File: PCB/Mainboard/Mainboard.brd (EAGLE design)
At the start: 39.1 x 39.1 mm, 18 parts

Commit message: Redesign
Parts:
- removed C3, C4, C5: 20nF, rcl:C0603
- removed DOWN, LEFT, RIGHT, UP: TASTER, button:TASTER
- removed MCU: ATTINY1614/16/17, ATTINY161x:QFN24-4X4
- removed U$1, U$2, U$3, U$4: MOLEX-STACKINGHEADER, Molex-53307-1071:53307-1071
- added JP1: (no value), pinhead:1X02/90
- added LED1, LED2: (no value), led:CHIP-LED0805
- added LEG_0: ATTINY1614, HeRo:SOIC14
- added R5, R6: (no value), rcl:R0805
- added SERVO_0: SERVO_X3, HeRo:2X03/90
- C1: value 100nF -> (none); device rcl:C0603 -> rcl:C0805
- C2: value 20nF -> (none); device rcl:C0603 -> rcl:C0805
- R1, R2, R3, R4: value 1k -> (none); device rcl:R0603 -> rcl:R0805
- moved R2 32.6 mm to (3.81, 4.45), turned to 0 degrees
- moved C1 25.7 mm to (8.26, 4.45), flipped to the top, turned to 180 degrees
- moved C2 17.3 mm to (17.1, 17.8)
- moved R4 13.0 mm to (15.6, 10.8), turned to 45 degrees
- moved R3 8.67 mm to (14.9, 13.3), turned to 45 degrees
- moved R1 6.99 mm to (12.7, 4.45), turned to 180 degrees
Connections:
- removed net ADD0: MCU.7, U$1.P$6
- removed net ADD1: MCU.8, U$1.P$7
- removed net ADD2: MCU.9, U$1.P$8
- removed net ADD3: MCU.10, U$1.P$9
- removed net DOWN: C3.1, MCU.20, R1.1
- removed net LEFT: C4.1, MCU.19, R3.1
- removed net N$3: R2.2, UP.A0, UP.A1
- removed net RIGHT: C5.1, MCU.18, R4.1
- removed net UP: C2.1, MCU.17, R2.1
- removed net UPDI: MCU.23, U$1.P$3
- new net ADDA_0: LEG_0.5, R3.1
- new net ADDB_0: LEG_0.4, R4.1
- new net ADDC_0: LEG_0.3, R5.1
- new net LEDA_0: LEG_0.2, R1.1
- new net LEDB_0: LEG_0.13, R2.1
- new net PWMA_0: LEG_0.9, SERVO_0.1
- new net PWMB_0: LEG_0.8, SERVO_0.2
- new net PWMC_0: LEG_0.7, SERVO_0.3
- new net SENSE_0: C2.1, LEG_0.6, R6.1
- new net UPDI_0: LEG_0.10
- new net VDD: SERVO_0.4, SERVO_0.5, SERVO_0.6
- net +5V: now also LEG_0.1; no longer MCU.4, U$1.P$1, U$2.P$1, U$3.P$1, U$4.P$1
- net GND: now also JP1.2, LED1.C, LED2.C, LEG_0.14, R3.2, R4.2, R5.2, SERVO_0.7, SERVO_0.8, SERVO_0.9; no longer C3.2, C4.2, C5.2, DOWN.B0, DOWN.B1, LEFT.B0, LEFT.B1, MCU.3, RIGHT.B0, RIGHT.B1, U$1.P$10, U$2.P$10, U$3.P$10, U$4.P$10, UP.B0, UP.B1
- net N$1: now also LED1.A; no longer DOWN.A0, DOWN.A1
- net N$2: now also LED2.A, R2.2; no longer LEFT.A0, LEFT.A1, R3.2
- net N$4: now also JP1.1, R6.2; no longer R4.2, RIGHT.A0, RIGHT.A1
- net SCL: now also LEG_0.12; no longer MCU.16, U$1.P$4
- net SDA: now also LEG_0.11; no longer MCU.15, U$1.P$5
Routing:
- net GND: track 58.3 -> 17.3 mm, vias 4 -> 6
- net DOWN: track 24.6 -> 0.00 mm, vias 1 -> 0
- net RIGHT: track 22.9 -> 0.00 mm, vias 1 -> 0
- net UP: track 18.7 -> 0.00 mm, vias 1 -> 0
- net UPDI: track 17.9 -> 0.00 mm, vias 2 -> 0
- net LEFT: track 16.3 -> 0.00 mm, vias 1 -> 0
- net N$3: track 12.0 -> 0.00 mm
- net +5V: track 15.0 -> 4.28 mm, vias 5 -> 0
- net N$1: track 12.1 -> 2.26 mm
- net N$2: track 12.0 -> 2.26 mm
- net N$4: track 11.9 -> 3.50 mm
- net SENSE_0: track 0.00 -> 8.21 mm
- net SCL: track 8.19 -> 0.00 mm
- net ADD3: track 6.72 -> 0.00 mm
- net PWMA_0: track 0.00 -> 5.80 mm
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- added copper zone on layer 1, net N$3
- added copper zone on layer 1, net VDD
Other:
- board size 39.1 x 39.1 mm -> 19.3 x 26.7 mm

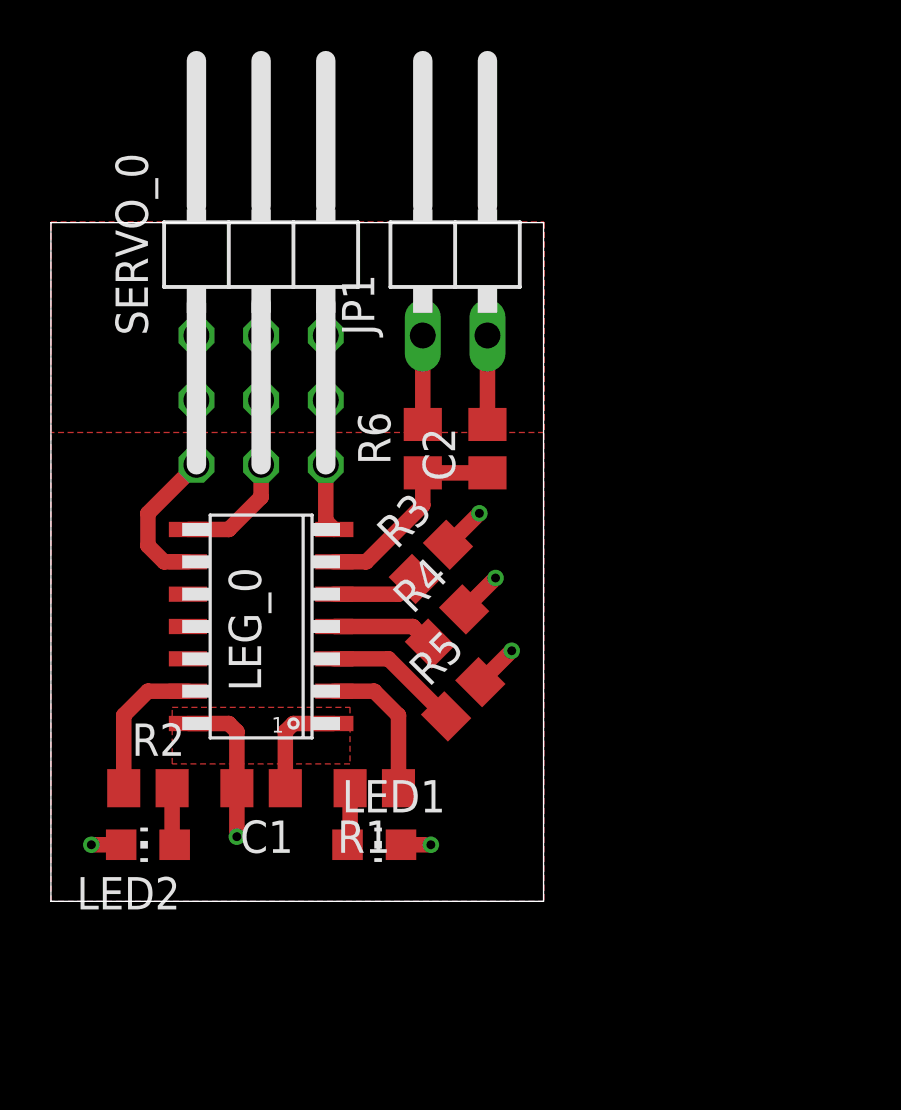
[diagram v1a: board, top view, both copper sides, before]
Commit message: Finished Servocontroller design
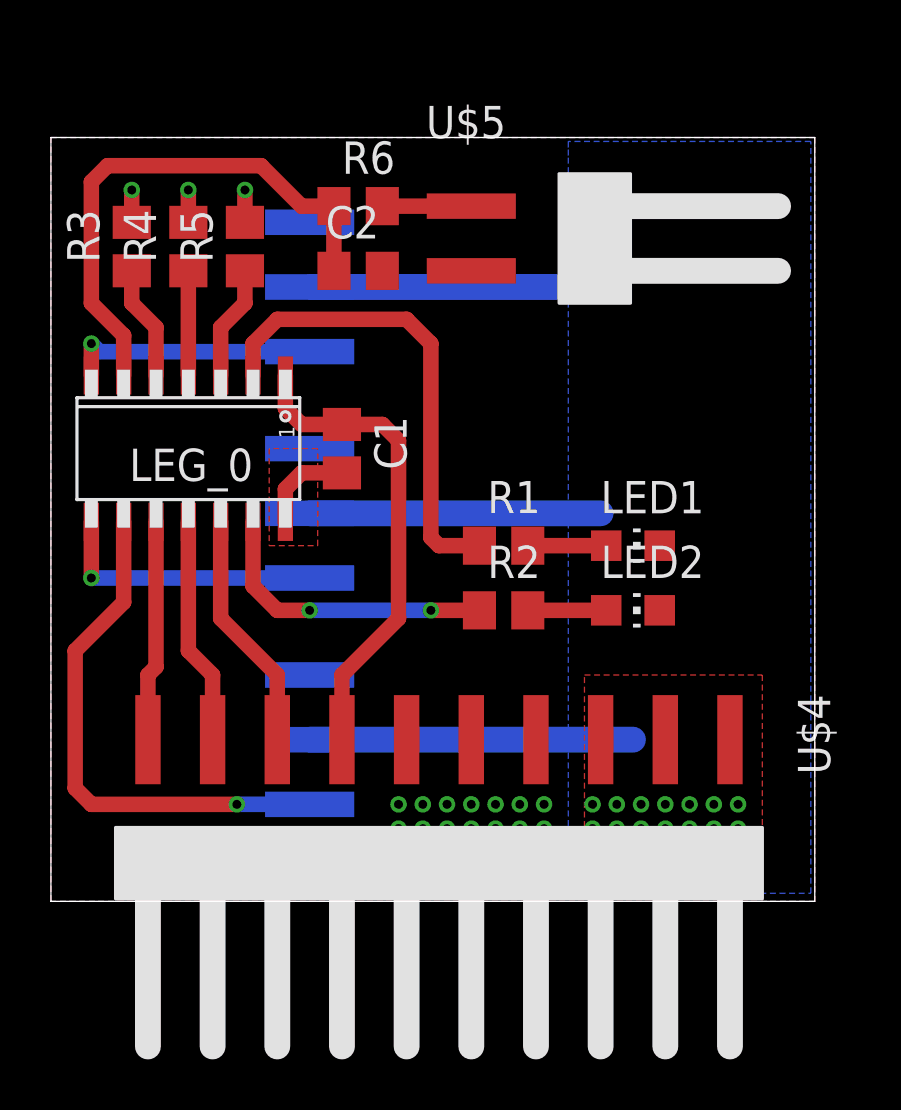
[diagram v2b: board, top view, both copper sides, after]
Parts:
- removed JP1: (no value), pinhead:1X02/90
- removed SERVO_0: SERVO_X3, HeRo:2X03/90
- added U$1, U$2, U$3: SERVO, HeRo:SL12SMD058
- added U$4: PINHEAD10SMD, HeRo:PINHD10SMD
- added U$5: PINHEAD2SMD, HeRo:PINHD2SMD
- moved LED2 21.2 mm to (22.9, 11.4), turned to 270 degrees
- moved R5 19.7 mm to (7.62, 25.7), turned to 90 degrees
- moved R4 18.1 mm to (5.40, 25.7), turned to 90 degrees
- moved R3 17.1 mm to (3.17, 25.7), turned to 90 degrees
- moved R2 15.6 mm to (17.8, 11.4)
- moved LED1 15.5 mm to (22.9, 14.0)
- moved C1 13.7 mm to (11.4, 17.8), turned to 270 degrees
- moved R1 10.8 mm to (17.8, 14.0), turned to 0 degrees
- moved R6 9.86 mm to (12.1, 27.3), turned to 0 degrees
- moved C2 8.64 mm to (12.1, 24.8), turned to 0 degrees
- moved LEG_0 7.55 mm to (5.40, 17.8), turned to 180 degrees
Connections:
- net +5V: now also U$4.7
- net GND: now also U$1.3, U$2.3, U$3.3, U$4.4, U$4.5, U$4.6, U$5.2; no longer JP1.2, SERVO_0.7, SERVO_0.8, SERVO_0.9
- net N$4: now also U$5.1; no longer JP1.1
- net PWMA_0: now also U$3.1; no longer SERVO_0.1
- net PWMB_0: now also U$2.1; no longer SERVO_0.2
- net PWMC_0: now also U$1.1; no longer SERVO_0.3
- net SCL: now also U$4.8
- net SDA: now also U$4.9
- net UPDI_0: now also U$4.10
- net VDD: now also U$1.2, U$2.2, U$3.2, U$4.1, U$4.2, U$4.3; no longer SERVO_0.4, SERVO_0.5, SERVO_0.6
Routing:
- net VDD: track 0.00 -> 35.6 mm, vias 0 -> 14
- net PWMA_0: track 5.80 -> 20.7 mm, vias 0 -> 1
- net +5V: track 4.28 -> 18.9 mm
- net LEDA_0: track 5.78 -> 18.7 mm
- net SENSE_0: track 8.21 -> 21.1 mm
- net GND: track 17.3 -> 7.59 mm, vias 6 -> 17
- net SCL: track 0.00 -> 9.48 mm
- net SDA: track 0.00 -> 8.95 mm
- net UPDI_0: track 0.00 -> 8.69 mm
- net PWMC_0: track 2.68 -> 9.96 mm, vias 0 -> 1
- net PWMB_0: track 4.67 -> 10.8 mm, vias 0 -> 1
- net LEDB_0: track 5.77 -> 11.8 mm, vias 0 -> 2
- net ADDA_0: track 3.37 -> 4.51 mm
- net ADDC_0: track 5.33 -> 4.51 mm
- net N$1: track 2.26 -> 3.08 mm
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- added copper zone on layer 1, net GND
- added copper zone on layer 16, net VDD
- removed copper zone on layer 1, net +5V
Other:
- board size 19.3 x 26.7 mm -> 30 x 30 mm

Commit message: Minor changes in controller, new mainboard
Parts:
- removed C1, C2: (no value), rcl:C0805
- removed LED1, LED2: (no value), led:CHIP-LED0805
- removed LEG_0: ATTINY1614, HeRo:SOIC14
- removed R1, R2, R3, R4, R5, R6: (no value), rcl:R0805
- removed U$2, U$3: SERVO, HeRo:SL12SMD058
- removed U$4: PINHEAD10SMD, HeRo:PINHD10SMD
- removed U$5: PINHEAD2SMD, HeRo:PINHD2SMD
- added LEG0, LEG1, LEG2, LEG3, LEG4, LEG5: (no value), pinhead:1X10
- U$1: value SERVO -> ESP32-DOITV1; device HeRo:SL12SMD058 -> HeRo:ESP32-DOITV1
- moved U$1 88.9 mm to (30.5, 111.8), turned to 90 degrees
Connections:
- removed net ADDA_0: LEG_0.5, R3.1
- removed net ADDB_0: LEG_0.4, R4.1
- removed net ADDC_0: LEG_0.3, R5.1
- removed net LEDA_0: LEG_0.2, R1.1
- removed net LEDB_0: LEG_0.13, R2.1
- removed net N$1: LED1.A, R1.2
- removed net N$2: LED2.A, R2.2
- removed net N$4: R6.2, U$5.1
- removed net PWMA_0: LEG_0.9, U$3.1
- removed net PWMB_0: LEG_0.8, U$2.1
- removed net PWMC_0: LEG_0.7, U$1.1
- removed net SENSE_0: C2.1, LEG_0.6, R6.1
- new net UPDI_1: LEG1.10
- new net UPDI_2: LEG2.10
- new net UPDI_3: LEG3.10
- new net UPDI_4: LEG4.10
- new net UPDI_5: LEG5.10
- net +5V: now also LEG0.7, LEG1.7, LEG2.7, LEG3.7, LEG4.7, LEG5.7; no longer C1.1, LEG_0.1, U$4.7
- net GND: now also LEG0.4, LEG0.5, LEG0.6, LEG1.4, LEG1.5, LEG1.6, LEG2.4, LEG2.5, LEG2.6, LEG3.4, LEG3.5, LEG3.6, LEG4.4, LEG4.5, LEG4.6, LEG5.4, LEG5.5, LEG5.6; no longer C1.2, C2.2, LED1.C, LED2.C, LEG_0.14, R3.2, R4.2, R5.2, U$1.3, U$2.3, U$3.3, U$4.4, U$4.5, U$4.6, U$5.2
- net SCL: now also LEG0.8, LEG1.8, LEG2.8, LEG3.8, LEG4.8, LEG5.8, U$1.29; no longer LEG_0.12, U$4.8
- net SDA: now also LEG0.9, LEG1.9, LEG2.9, LEG3.9, LEG4.9, LEG5.9, U$1.26; no longer LEG_0.11, U$4.9
- net UPDI_0: now also LEG0.10; no longer LEG_0.10, U$4.10
- net VDD: now also LEG0.1, LEG0.2, LEG0.3, LEG1.1, LEG1.2, LEG1.3, LEG2.1, LEG2.2, LEG2.3, LEG3.1, LEG3.2, LEG3.3, LEG4.1, LEG4.2, LEG4.3, LEG5.1, LEG5.2, LEG5.3; no longer U$1.2, U$2.2, U$3.2, U$4.1, U$4.2, U$4.3
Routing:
- net SCL: track 9.48 -> 334.4 mm, vias 0 -> 6
- net SDA: track 8.95 -> 330.6 mm, vias 0 -> 6
- net VDD: track 35.6 -> 0.00 mm, vias 14 -> 0
- net SENSE_0: track 21.1 -> 0.00 mm
- net PWMA_0: track 20.7 -> 0.00 mm, vias 1 -> 0
- net +5V: track 18.9 -> 0.00 mm
- net LEDA_0: track 18.7 -> 0.00 mm
- net LEDB_0: track 11.8 -> 0.00 mm, vias 2 -> 0
- net PWMB_0: track 10.8 -> 0.00 mm, vias 1 -> 0
- net PWMC_0: track 9.96 -> 0.00 mm, vias 1 -> 0
- net UPDI_0: track 8.69 -> 0.00 mm
- net GND: track 7.59 -> 0.00 mm, vias 17 -> 0
- net ADDC_0: track 4.51 -> 0.00 mm
- net ADDA_0: track 4.51 -> 0.00 mm
- net ADDB_0: track 4.11 -> 0.00 mm
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- removed copper zone on layer 1, net GND
- removed copper zone on layer 1, net N$3
- removed copper zone on layer 16, net VDD
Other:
- board size 30 x 30 mm -> 60 x 140 mm
- board text added: "Controller v0.1"
- board text added: "HeRo Mini"
- board text added: "https://github.com/xXAM22Xx/HeRo-Mini"

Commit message: WIP Mainboard design
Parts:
- added I2C-PWR-SELECT: (no value), pinhead:1X03
- added JP1, JP2: (no value), pinhead:1X18
- added PWR-SELECT: (no value), pinhead:2X03
- added R1, R2: 10k, rcl:R0805
- added U$2: D24V150F6, HeRo:D24V150F6
- moved LEG5 11.3 mm to (58.0, 137.0)
- moved LEG0 11.3 mm to (2.00, 137.0)
- moved U$1 9.25 mm to (30.0, 121.0)
- moved LEG3 1.29 mm to (58.0, 13.0)
- moved LEG2 1.11 mm to (2.00, 13.0)
- moved LEG4 0.85 mm to (58.0, 70.0)
- moved LEG1 0.54 mm to (2.00, 70.0)
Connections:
- removed net UPDI_0: LEG0.10
- removed net UPDI_1: LEG1.10
- removed net UPDI_2: LEG2.10
- removed net UPDI_3: LEG3.10
- removed net UPDI_4: LEG4.10
- removed net UPDI_5: LEG5.10
- new net 3V3-1: I2C-PWR-SELECT.1, JP1.15, U$1.22
- new net 3V3-2: I2C-PWR-SELECT.3, JP1.18, U$1.19
- new net GND1: JP2.14, PWR-SELECT.2, U$1.5
- new net GND2: JP2.17, PWR-SELECT.6, U$1.2
- new net N$1: I2C-PWR-SELECT.2, R1.2, R2.2
- new net N$10: JP2.9, U$1.10
- new net N$11: JP2.10, U$1.9
- new net N$12: JP2.11, U$1.8
- new net N$13: JP2.12, U$1.7
- new net N$14: JP2.13, U$1.6
- new net N$15: JP2.16, U$1.3
- new net N$16: JP1.17, U$1.20
- new net N$17: JP1.16, U$1.21
- new net N$18: JP1.14, U$1.23
- new net N$19: JP1.13, U$1.24
- new net N$2: JP2.1, U$1.18
- new net N$20: JP1.12, U$1.25
- new net N$21: JP1.11, U$1.26
- new net N$22: JP1.10, U$1.27
- new net N$23: JP1.9, U$1.28
- new net N$24: JP1.8, U$1.29
- new net N$25: JP1.7, U$1.30
- new net N$26: JP1.6, U$1.31
- new net N$27: JP1.4, U$1.33
- new net N$28: JP1.3, U$1.34
- new net N$29: JP1.1, U$1.36
- new net N$3: JP2.2, U$1.17
- new net N$4: JP2.3, U$1.16
- new net N$5: JP2.4, U$1.15
- new net N$6: JP2.5, U$1.14
- new net N$7: JP2.6, U$1.13
- new net N$8: JP2.7, U$1.12
- new net N$9: JP2.8, U$1.11
- new net VCC1: JP2.15, PWR-SELECT.1, U$1.4
- new net VCC2: JP2.18, PWR-SELECT.5, U$1.1
- net +5V: now also LEG0.4, LEG1.4, LEG2.4, LEG3.4, LEG4.4, LEG5.4, PWR-SELECT.3; no longer LEG0.7, LEG1.7, LEG2.7, LEG3.7, LEG4.7, LEG5.7
- net GND: now also LEG0.10, LEG0.8, LEG0.9, LEG1.10, LEG1.8, LEG1.9, LEG2.10, LEG2.8, LEG2.9, LEG3.10, LEG3.8, LEG3.9, LEG4.10, LEG4.8, LEG4.9, LEG5.10, LEG5.8, LEG5.9, PWR-SELECT.4; no longer LEG0.4, LEG0.5, LEG0.6, LEG1.4, LEG1.5, LEG1.6, LEG2.4, LEG2.5, LEG2.6, LEG3.4, LEG3.5, LEG3.6, LEG4.4, LEG4.5, LEG4.6, LEG5.4, LEG5.5, LEG5.6
- net SCL: now also JP1.2, LEG0.5, LEG1.5, LEG2.5, LEG3.5, LEG4.5, LEG5.5, R2.1, U$1.35; no longer LEG0.8, LEG1.8, LEG2.8, LEG3.8, LEG4.8, LEG5.8, U$1.29
- net SDA: now also JP1.5, LEG0.6, LEG1.6, LEG2.6, LEG3.6, LEG4.6, LEG5.6, R1.1, U$1.32; no longer LEG0.9, LEG1.9, LEG2.9, LEG3.9, LEG4.9, LEG5.9, U$1.26
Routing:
- net SCL: track 334.4 -> 414.6 mm, vias 6 -> 8
- net SDA: track 330.6 -> 408.9 mm
- net VCC1: track 0.00 -> 11.5 mm
- net VCC2: track 0.00 -> 11.1 mm
- net GND1: track 0.00 -> 10.1 mm
- net 3V3-2: track 0.00 -> 9.85 mm
- net 3V3-1: track 0.00 -> 9.28 mm
- net GND2: track 0.00 -> 8.01 mm
- net +5V: track 0.00 -> 6.73 mm, vias 0 -> 1
- net N$1: track 0.00 -> 6.53 mm
- net N$9: track 0.00 -> 3.74 mm
- net N$8: track 0.00 -> 3.74 mm
- net N$7: track 0.00 -> 3.74 mm
- net N$6: track 0.00 -> 3.74 mm
- net N$5: track 0.00 -> 3.74 mm
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- added copper zone on layer 1, net +5V
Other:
- board size 60 x 140 mm -> 60 x 150 mm
- board text added: "TODO: move middle connectors"

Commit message: Minor Changes
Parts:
- added U$3: GY-521_MPU6050, HeRo:GY-521_MPU6050
- added U$4: VL53L0XV, HeRo:VL53L0X_V
- added U$5: D24V10F5, HeRo:D24V10F5
- moved U$2 63.4 mm to (30.0, 28.0)
- moved I2C-PWR-SELECT 34.0 mm to (13.0, 139.0), turned to 90 degrees
- moved R2 34.0 mm to (9.00, 137.0), turned to 0 degrees
- moved PWR-SELECT 33.0 mm to (48.0, 138.0), turned to 90 degrees
- moved R1 33.0 mm to (9.00, 141.0), turned to 0 degrees
- moved JP1 2.00 mm to (21.0, 120.0), flipped to the bottom, turned to 90 degrees
- moved JP2 2.00 mm to (39.0, 120.0), turned to 90 degrees
- flipped U$1 to the top, turned to 270 degrees
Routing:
- net SCL: track 414.6 -> 0.00 mm, vias 8 -> 0
- net SDA: track 408.9 -> 0.00 mm, vias 6 -> 0
- net VCC1: track 11.5 -> 0.00 mm
- net VCC2: track 11.1 -> 0.00 mm
- net GND1: track 10.1 -> 0.00 mm
- net 3V3-2: track 9.85 -> 0.00 mm
- net 3V3-1: track 9.28 -> 0.00 mm
- net GND2: track 8.01 -> 0.00 mm
- net +5V: track 6.73 -> 0.00 mm, vias 1 -> 0
- net N$1: track 6.53 -> 0.00 mm
- net N$9: track 3.74 -> 0.00 mm
- net N$8: track 3.74 -> 0.00 mm
- net N$7: track 3.74 -> 0.00 mm
- net N$6: track 3.74 -> 0.00 mm
- net N$5: track 3.74 -> 0.00 mm
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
